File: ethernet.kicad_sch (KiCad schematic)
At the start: 1 part, among them J1 8P8C_LED_Shielded

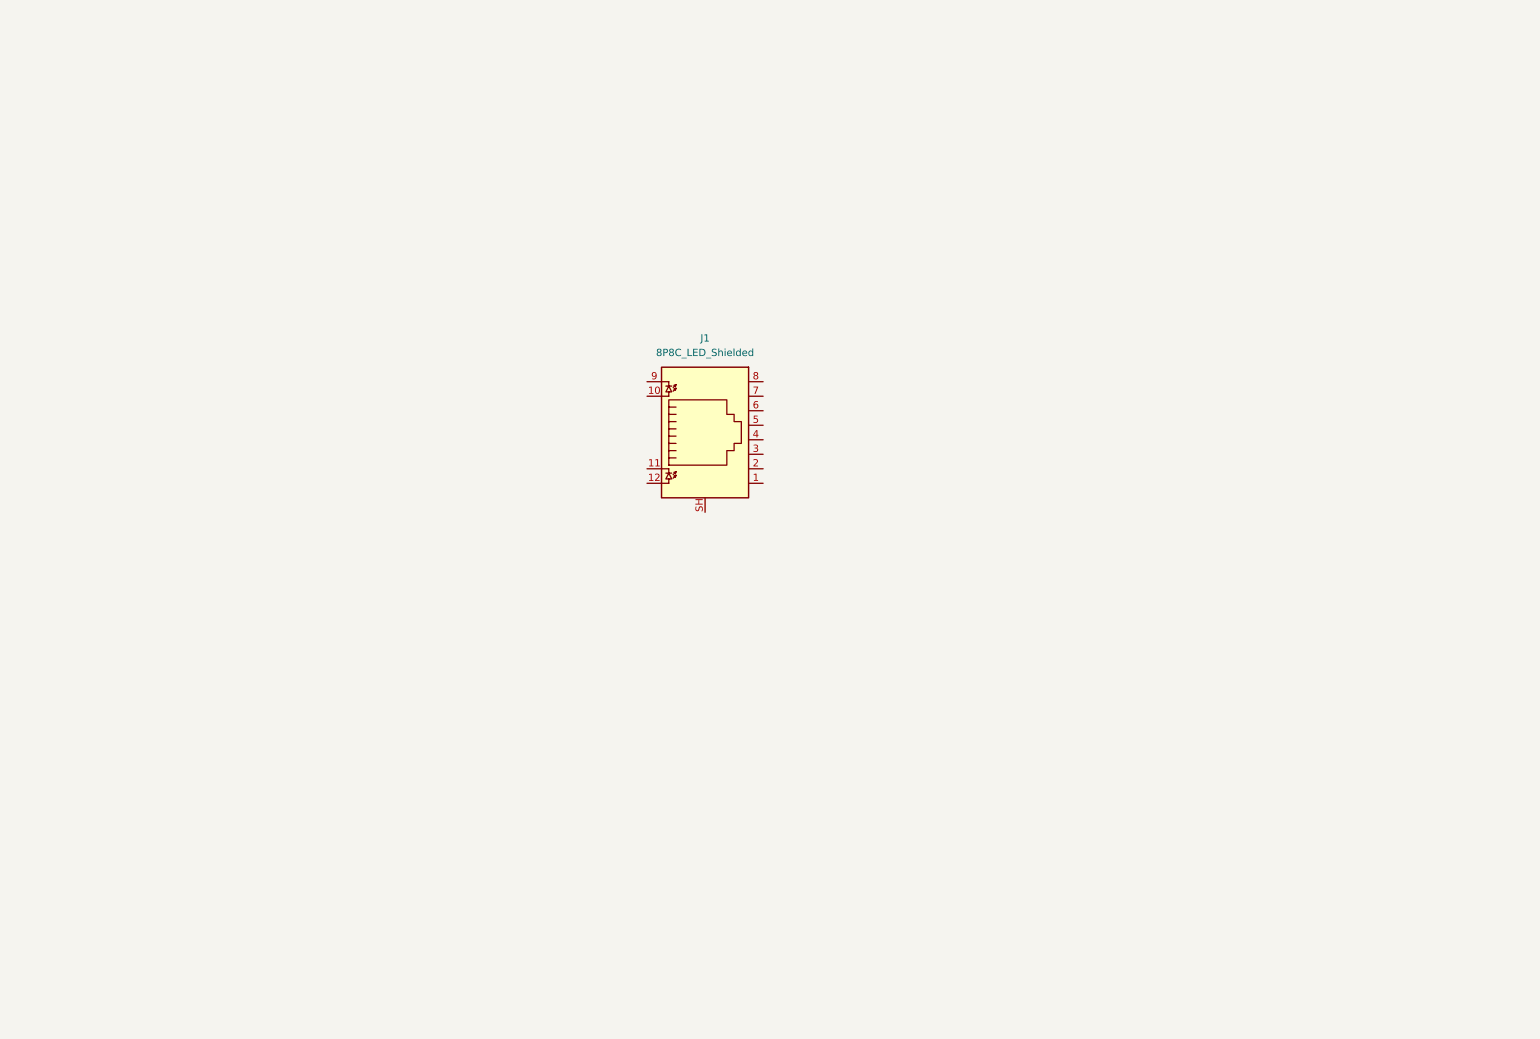
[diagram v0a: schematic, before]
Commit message: add POE schematics, Ethernet phy
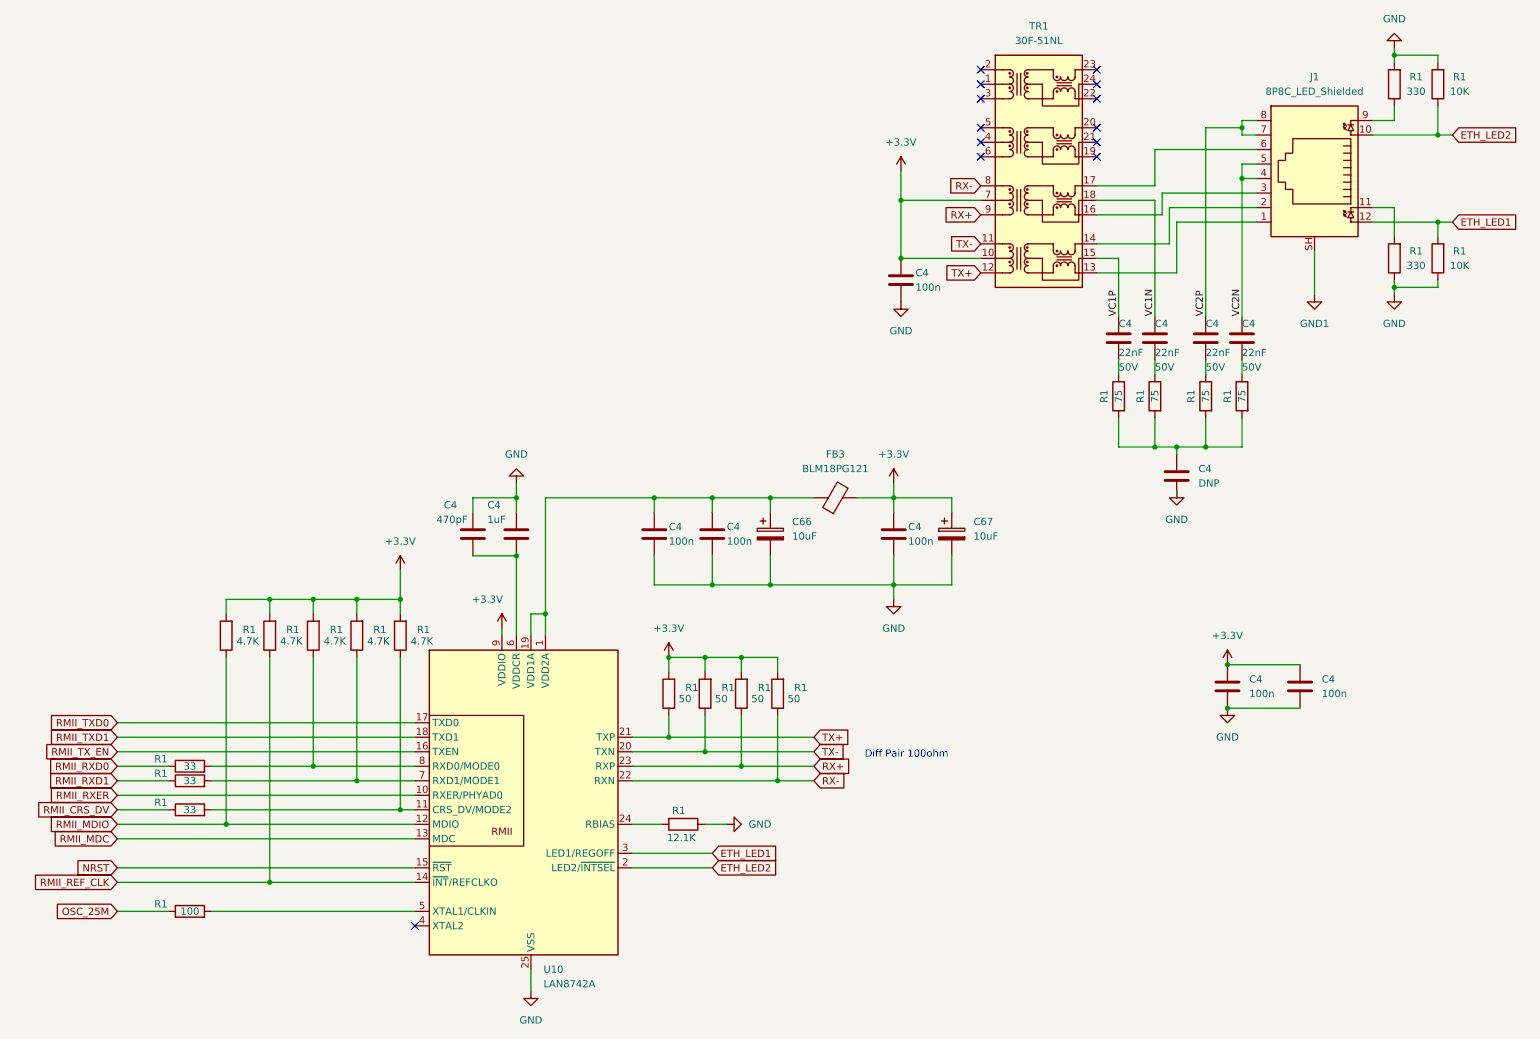
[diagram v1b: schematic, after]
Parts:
- added C4: DNP, Capacitor_SMD:C_0402_1005Metric, symbol Device:C
- added C4 (x4): 22nF, Capacitor_SMD:C_0603_1608Metric, symbol Device:C
- added C4: 1uF, Capacitor_SMD:C_0402_1005Metric, symbol Device:C
- added C4 (x6): 100n, Capacitor_SMD:C_0402_1005Metric, symbol Device:C
- added C4: 470pF, Capacitor_SMD:C_0402_1005Metric, symbol Device:C
- added C66, C67: 10uF, Capacitor_Tantalum_SMD:CP_EIA-3216-18_Kemet-A, symbol Device:C_Polarized
- added FB3: BLM18PG121, Inductor_SMD:L_0603_1608Metric, symbol Device:FerriteBead
- added R1 (x5): 4.7K, Resistor_SMD:R_0402_1005Metric, symbol Device:R
- added R1 (x4): 50, Resistor_SMD:R_0402_1005Metric, symbol Device:R
- added R1 (x4): 75, Resistor_SMD:R_0402_1005Metric, symbol Device:R
- added R1 (x3): 33, Resistor_SMD:R_0402_1005Metric, symbol Device:R
- added R1 (x2): 10K, Resistor_SMD:R_0402_1005Metric, symbol Device:R
- added R1: 100, Resistor_SMD:R_0402_1005Metric, symbol Device:R
- added R1: 12.1K, Resistor_SMD:R_0402_1005Metric, symbol Device:R
- added R1 (x2): 330, Resistor_SMD:R_0402_1005Metric, symbol Device:R
- added TR1: 30F-51NL, Transformer_SMD:Transformer_Ethernet_YDS_30F-51NL_SO-24_7.1x15.1mm, symbol Transformer:30F-51NL
- added U10: LAN8742A, Package_DFN_QFN:VQFN-24-1EP_4x4mm_P0.5mm_EP2.5x2.5mm_ThermalVias, symbol Interface_Ethernet:LAN8742A
- J1: footprint (none) -> Connector_RJ:RJ45_Amphenol_RJHSE538X
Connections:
- net at J1.1: now also TR1.13 (MX4-)
- net ETH_LED2: now reaches J1.10
- net ETH_LED2: now also R1.1, U10.2 (LED2/~{INTSEL})
- net at J1.11: now also R1.2
- net ETH_LED1: now reaches J1.12
- net ETH_LED1: now also R1.2, U10.3 (LED1/REGOFF)
- net at J1.2: now also TR1.14 (MX4+)
- net at J1.3: now also TR1.16 (MX3-)
- net VC2N: now reaches J1.4
- net VC2N: now also J1.5, C4.2
- net at J1.6: now also TR1.17 (MX3+)
- net VC2P: now reaches J1.7
- net VC2P: now also J1.8, C4.2
- net at J1.9: now also R1.1
- net GND1: now reaches J1.SH
- new net: C4.1, R1.2, R1.2, R1.2, R1.2
- new net: C4.1, R1.1 (x4)
- new net: C4.1, C4.1, C66.1, FB3.1, U10.1 (VDD2A), U10.19 (VDD1A)
- new net: R1.1, R1.2, U10.11 (CRS_DV/MODE2)
- new net: R1.2, U10.24 (RBIAS)
- new net: R1.2, U10.5 (XTAL1/CLKIN)
- new net: C4.2, C4.2, U10.6 (VDDCR)
- new net: R1.1, R1.2, U10.7 (RXD1/MODE1)
- new net: R1.1, R1.2, U10.8 (RXD0/MODE0)
- new net +3.3V: C4.1, C4.1, C4.1, C4.1, C67.1, FB3.2, R1.2, R1.2, R1.2, R1.2, R1.2, R1.2, R1.2, R1.2, R1.2, TR1.10 (CT), TR1.7 (CT), U10.9 (VDDIO)
- new net GND: C4.1, C4.1, C4.2, C4.2, C4.2, C4.2, C4.2, C4.2, C4.2, C66.2, C67.2, R1.1, R1.1, R1.1, R1.2, R1.2, U10.25 (VSS)
- new net NRST: U10.15 (~{RST})
- new net OSC_25M: R1.1
- new net RMII_CRS_DV: R1.1
- new net RMII_MDC: U10.13 (MDC)
- new net RMII_MDIO: R1.1, U10.12 (MDIO)
- new net RMII_REF_CLK: R1.1, U10.14 (~{INT}/REFCLKO)
- new net RMII_RXD0: R1.1
- new net RMII_RXD1: R1.1
- new net RMII_RXER: U10.10 (RXER/PHYAD0)
- new net RMII_TXD0: U10.17 (TXD0)
- new net RMII_TXD1: U10.18 (TXD1)
- new net RMII_TX_EN: U10.16 (TXEN)
- new net RX+: R1.1, TR1.9 (TD3-), U10.23 (RXP)
- new net RX-: R1.1, TR1.8 (TD3+), U10.22 (RXN)
- new net TX+: R1.1, TR1.12 (TD4-), U10.21 (TXP)
- new net TX-: R1.1, TR1.11 (TD4+), U10.20 (TXN)
- new net VC1N: C4.2, TR1.18 (CT)
- new net VC1P: C4.2, TR1.15 (CT)
- no-connect marks 0 -> 13
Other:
- note added: "Diff Pair 100ohm"
- moved on the sheet: J1

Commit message: almost final schematics
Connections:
- net GND: no longer C4.2
- net GND1: now also C4.2
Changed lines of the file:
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@@
   (junction (at 228.6 46.99) (diameter 0) (color 0 0 0 0)
   )
+  (junction (at 222.25 67.31) (diameter 0) (color 0 0 0 0)
+  )
   (junction (at 262.89 54.61) (diameter 0) (color 0 0 0 0)
   )
@@
   (junction (at 134.62 147.32) (diameter 0) (color 0 0 0 0)
   )
+  (junction (at 207.01 69.85) (diameter 0) (color 0 0 0 0)
+  )
   (junction (at 125.73 102.87) (diameter 0) (color 0 0 0 0)
   )
@@
   (junction (at 73.66 152.4) (diameter 0) (color 0 0 0 0)
   )
+  (junction (at 213.36 67.31) (diameter 0) (color 0 0 0 0)
+  )
   (junction (at 226.06 132.08) (diameter 0) (color 0 0 0 0)
   )
@@
   )
   (junction (at 140.97 130.81) (diameter 0) (color 0 0 0 0)
+  )
+  (junction (at 228.6 69.85) (diameter 0) (color 0 0 0 0)
   )
   (junction (at 222.25 93.98) (diameter 0) (color 0 0 0 0)
@@
     (stroke (width 0) (type default))
   )
-  (wire (pts (xy 207.01 60.96) (xy 207.01 71.12))
-    (stroke (width 0) (type default))
-  )
-  (wire (pts (xy 217.17 102.87) (xy 217.17 101.6))
+  (wire (pts (xy 207.01 60.96) (xy 207.01 69.85))
     (stroke (width 0) (type default))
   )
@@
     (stroke (width 0) (type default))
   )
+  (wire (pts (xy 199.39 82.55) (xy 199.39 69.85))
+    (stroke (width 0) (type default))
+  )
   (wire (pts (xy 106.68 102.87) (xy 125.73 102.87))
     (stroke (width 0) (type default))
@@
     (stroke (width 0) (type default))
   )
+  (wire (pts (xy 207.01 69.85) (xy 207.01 71.12))
+    (stroke (width 0) (type default))
+  )
   (wire (pts (xy 213.36 50.8) (xy 203.2 50.8))
     (stroke (width 0) (type default))
@@
     (stroke (width 0) (type default))
   )
-  (wire (pts (xy 213.36 50.8) (xy 213.36 71.12))
+  (wire (pts (xy 213.36 50.8) (xy 213.36 67.31))
     (stroke (width 0) (type default))
   )
@@
     (stroke (width 0) (type default))
   )
+  (wire (pts (xy 237.49 69.85) (xy 228.6 69.85))
+    (stroke (width 0) (type default))
+  )
   (wire (pts (xy 228.6 93.98) (xy 222.25 93.98))
     (stroke (width 0) (type default))
@@
     (stroke (width 0) (type default))
   )
+  (wire (pts (xy 241.3 82.55) (xy 241.3 67.31))
+    (stroke (width 0) (type default))
+  )
   (wire (pts (xy 104.14 127) (xy 104.14 123.19))
     (stroke (width 0) (type default))
@@
     (stroke (width 0) (type default))
   )
+  (wire (pts (xy 228.6 46.99) (xy 228.6 69.85))
+    (stroke (width 0) (type default))
+  )
   (wire (pts (xy 134.62 133.35) (xy 134.62 130.81))
     (stroke (width 0) (type default))
@@
     (stroke (width 0) (type default))
   )
+  (wire (pts (xy 195.58 82.55) (xy 195.58 67.31))
+    (stroke (width 0) (type default))
+  )
   (wire (pts (xy 168.91 60.96) (xy 168.91 50.8))
     (stroke (width 0) (type default))
@@
     (stroke (width 0) (type default))
   )
+  (wire (pts (xy 241.3 67.31) (xy 222.25 67.31))
+    (stroke (width 0) (type default))
+  )
   (wire (pts (xy 48.26 149.86) (xy 66.04 149.86))
     (stroke (width 0) (type default))
   )
+  (wire (pts (xy 228.6 69.85) (xy 228.6 71.12))
+    (stroke (width 0) (type default))
+  )
   (wire (pts (xy 121.92 152.4) (xy 147.32 152.4))
     (stroke (width 0) (type default))
@@
     (stroke (width 0) (type default))
   )
+  (wire (pts (xy 199.39 69.85) (xy 207.01 69.85))
+    (stroke (width 0) (type default))
+  )
   (wire (pts (xy 147.32 140.97) (xy 147.32 152.4))
     (stroke (width 0) (type default))
@@
     (stroke (width 0) (type default))
   )
-  (wire (pts (xy 228.6 46.99) (xy 228.6 71.12))
-    (stroke (width 0) (type default))
-  )
   (wire (pts (xy 262.89 54.61) (xy 265.43 54.61))
     (stroke (width 0) (type default))
@@
     (stroke (width 0) (type default))
   )
+  (wire (pts (xy 195.58 67.31) (xy 213.36 67.31))
+    (stroke (width 0) (type default))
+  )
   (wire (pts (xy 31.75 157.48) (xy 40.64 157.48))
     (stroke (width 0) (type default))
@@
     (stroke (width 0) (type default))
   )
-  (wire (pts (xy 241.3 59.69) (xy 241.3 67.31))
-    (stroke (width 0) (type default))
-  )
   (wire (pts (xy 228.6 88.9) (xy 228.6 93.98))
     (stroke (width 0) (type default))
@@
     (stroke (width 0) (type default))
   )
+  (wire (pts (xy 222.25 67.31) (xy 222.25 71.12))
+    (stroke (width 0) (type default))
+  )
   (wire (pts (xy 262.89 34.29) (xy 262.89 39.37))
     (stroke (width 0) (type default))
@@
     (stroke (width 0) (type default))
   )
+  (wire (pts (xy 237.49 82.55) (xy 237.49 69.85))
+    (stroke (width 0) (type default))
+  )
   (wire (pts (xy 213.36 93.98) (xy 213.36 88.9))
     (stroke (width 0) (type default))
   )
-  (wire (pts (xy 222.25 38.1) (xy 222.25 71.12))
+  (wire (pts (xy 222.25 38.1) (xy 222.25 67.31))
     (stroke (width 0) (type default))
   )
@@
     (stroke (width 0) (type default))
   )
+  (wire (pts (xy 213.36 67.31) (xy 213.36 71.12))
+    (stroke (width 0) (type default))
+  )
   (wire (pts (xy 135.89 118.11) (xy 146.05 118.11))
     (stroke (width 0) (type default))
   )
   (text "Diff Pair 100ohm" (at 162.56 148.59 0)
-    (effects (font (size 1.27 1.27)) (justify left bottom))
-  )
-  (label "VC2N" (at 228.6 71.12 90) (fields_autoplaced)
-    (effects (font (size 1.27 1.27)) (justify left bottom))
-  )
-  (label "VC1N" (at 213.36 71.12 90) (fields_autoplaced)
-    (effects (font (size 1.27 1.27)) (justify left bottom))
-  )
-  (label "VC1P" (at 207.01 71.12 90) (fields_autoplaced)
-    (effects (font (size 1.27 1.27)) (justify left bottom))
-  )
-  (label "VC2P" (at 222.25 71.12 90) (fields_autoplaced)
     (effects (font (size 1.27 1.27)) (justify left bottom))
   )
@@
     )
   )
+  (global_label "VC1P" (shape input) (at 199.39 82.55 270) (fields_autoplaced)
+    (effects (font (size 1.27 1.27)) (justify right))
+    (property "Intersheetrefs" "${INTERSHEET_REFS}" (at 199.39 90.3733 90)
+      (effects (font (size 1.27 1.27)) (justify right) hide)
+    )
+  )
   (global_label "ETH_LED1" (shape input) (at 135.89 165.1 0) (fields_autoplaced)
     (effects (font (size 1.27 1.27)) (justify left))
@@
     )
   )
+  (global_label "VC2N" (shape input) (at 237.49 82.55 270) (fields_autoplaced)
+    (effects (font (size 1.27 1.27)) (justify right))
+    (property "Intersheetrefs" "${INTERSHEET_REFS}" (at 237.49 90.4338 90)
+      (effects (font (size 1.27 1.27)) (justify right) hide)
+    )
+  )
+  (global_label "VC1N" (shape input) (at 195.58 82.55 270) (fields_autoplaced)
+    (effects (font (size 1.27 1.27)) (justify right))
+    (property "Intersheetrefs" "${INTERSHEET_REFS}" (at 195.58 90.4338 90)
+      (effects (font (size 1.27 1.27)) (justify right) hide)
+    )
+  )
   (global_label "ETH_LED1" (shape input) (at 265.43 54.61 0) (fields_autoplaced)
     (effects (font (size 1.27 1.27)) (justify left))
@@
     (effects (font (size 1.27 1.27)) (justify right))
     (property "Intersheetrefs" "${INTERSHEET_REFS}" (at 15.8229 170.18 0)
+      (effects (font (size 1.27 1.27)) (justify right) hide)
+    )
+  )
+  (global_label "VC2P" (shape input) (at 241.3 82.55 270) (fields_autoplaced)
+    (effects (font (size 1.27 1.27)) (justify right))
+    (property "Intersheetrefs" "${INTERSHEET_REFS}" (at 241.3 90.3733 90)
       (effects (font (size 1.27 1.27)) (justify right) hide)
     )
@@
     )
   )
+  (symbol (lib_id "power:GND1") (at 217.17 102.87 0) (unit 1)
+    (in_bom yes) (on_board yes) (dnp no) (fields_autoplaced)
+    (property "Reference" "#PWR045" (at 217.17 109.22 0)
+      (effects (font (size 1.27 1.27)) hide)
+    )
+    (property "Value" "GND1" (at 217.17 107.95 0)
+      (effects (font (size 1.27 1.27)))
+    )
+    (property "Footprint" "" (at 217.17 102.87 0)
+      (effects (font (size 1.27 1.27)) hide)
+    )
+    (property "Datasheet" "" (at 217.17 102.87 0)
+      (effects (font (size 1.27 1.27)) hide)
+    )
+    (pin "1")
+    (instances
+      (project "stm32f745-eth-can-sdram"
+        (path "/2fe210a3-bd39-4a0d-882e-a71d33b1f0de/4e4d7780-6fb5-4a29-9d61-bcff1bad1111"
+          (reference "#PWR045") (unit 1)
+        )
+        (path "/2fe210a3-bd39-4a0d-882e-a71d33b1f0de/36a88d0a-654b-478a-adb0-3744b540e62b"
+          (reference "#PWR01") (unit 1)
+        )
+      )
+    )
+  )
   (symbol (lib_id "Device:R") (at 44.45 149.86 90) (unit 1)
     (in_bom yes) (on_board yes) (dnp no)
@@
     )
   )
-  (symbol (lib_id "power:GND1") (at 241.3 67.31 0) (unit 1)
+  (symbol (lib_id "power:GND1") (at 241.3 59.69 0) (unit 1)
     (in_bom yes) (on_board yes) (dnp no) (fields_autoplaced)
-    (property "Reference" "#PWR045" (at 241.3 73.66 0)
-      (effects (font (size 1.27 1.27)) hide)
-    )
-    (property "Value" "GND1" (at 241.3 72.39 0)
-      (effects (font (size 1.27 1.27)))
-    )
-    (property "Footprint" "" (at 241.3 67.31 0)
-      (effects (font (size 1.27 1.27)) hide)
-    )
-    (property "Datasheet" "" (at 241.3 67.31 0)
+    (property "Reference" "#PWR045" (at 241.3 66.04 0)
+      (effects (font (size 1.27 1.27)) hide)
+    )
+    (property "Value" "GND1" (at 241.3 64.77 0)
+      (effects (font (size 1.27 1.27)))
+    )
+    (property "Footprint" "" (at 241.3 59.69 0)
+      (effects (font (size 1.27 1.27)) hide)
+    )
+    (property "Datasheet" "" (at 241.3 59.69 0)
       (effects (font (size 1.27 1.27)) hide)
     )
@@
         )
       )
-    )
-  )
-  (symbol (lib_id "power:GND") (at 217.17 101.6 0) (unit 1)
-    (in_bom yes) (on_board yes) (dnp no) (fields_autoplaced)
-    (property "Reference" "#PWR01" (at 217.17 107.95 0)
-      (effects (font (size 1.27 1.27)) hide)
-    )
-    (property "Value" "GND" (at 217.17 106.68 0)
-      (effects (font (size 1.27 1.27)))
-    )
-    (property "Footprint" "" (at 217.17 101.6 0)
-      (effects (font (size 1.27 1.27)) hide)
-    )
-    (property "Datasheet" "" (at 217.17 101.6 0)
-      (effects (font (size 1.27 1.27)) hide)
-    )
-    (pin "1")
-    (instances
-      (project "stm32f745-eth-can-sdram"
-        (path "/2fe210a3-bd39-4a0d-882e-a71d33b1f0de/36a88d0a-654b-478a-adb0-3744b540e62b"
-          (reference "#PWR01") (unit 1)
-        )
-      )
